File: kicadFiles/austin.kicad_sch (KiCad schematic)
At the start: 553 parts, among them J1 ARM SWD, J2 TYPE-C-31-M12_13, J3 Conn_01x04, Q1 AO3401A, Q2 DTC123JKAT146, Q3 DTC123J, SW1 MXSwitch, SW10 MXSwitch, SW100 MXSwitch, SW101 MXSwitch, SW102 MXSwitch, SW103 MXSwitch, SW104 MXSwitch, SW105 MXSwitch, SW106 MXSwitch, SW107 MXSwitch, SW108 MXSwitch, SW109 MXSwitch, SW11 MXSwitch, SW110 MXSwitch, SW111 MXSwitch, SW112 MXSwitch, SW113 MXSwitch, SW114 MXSwitch, SW12 MXSwitch, SW13 MXSwitch, SW14 MXSwitch, SW15 MXSwitch, SW16 MXSwitch, SW17 MXSwitch, SW18 MXSwitch, SW19 MXSwitch, SW2 MXSwitch, SW20 MXSwitch, SW21 MXSwitch, SW22 MXSwitch, SW23 MXSwitch, SW24 MXSwitch, SW25 MXSwitch, SW26 MXSwitch, SW27 MXSwitch, SW28 MXSwitch, SW29 MXSwitch, SW3 MXSwitch, SW30 MXSwitch, SW31 MXSwitch, SW32 MXSwitch, SW33 MXSwitch, SW34 MXSwitch, SW35 MXSwitch, SW36 MXSwitch, SW37 MXSwitch, SW38 MXSwitch, SW39 MXSwitch, SW4 MXSwitch, SW40 MXSwitch, SW41 MXSwitch, SW42 MXSwitch, SW43 MXSwitch, SW44 MXSwitch, SW45 MXSwitch, SW46 MXSwitch, SW47 MXSwitch, SW48 MXSwitch, SW49 MXSwitch, SW5 MXSwitch, SW50 MXSwitch, SW51 MXSwitch, SW52 MXSwitch, SW53 MXSwitch, SW54 MXSwitch, SW55 MXSwitch, SW56 MXSwitch, SW57 MXSwitch, SW58 MXSwitch, SW59 MXSwitch, SW6 MXSwitch, SW60 MXSwitch, SW61 MXSwitch, SW62 MXSwitch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

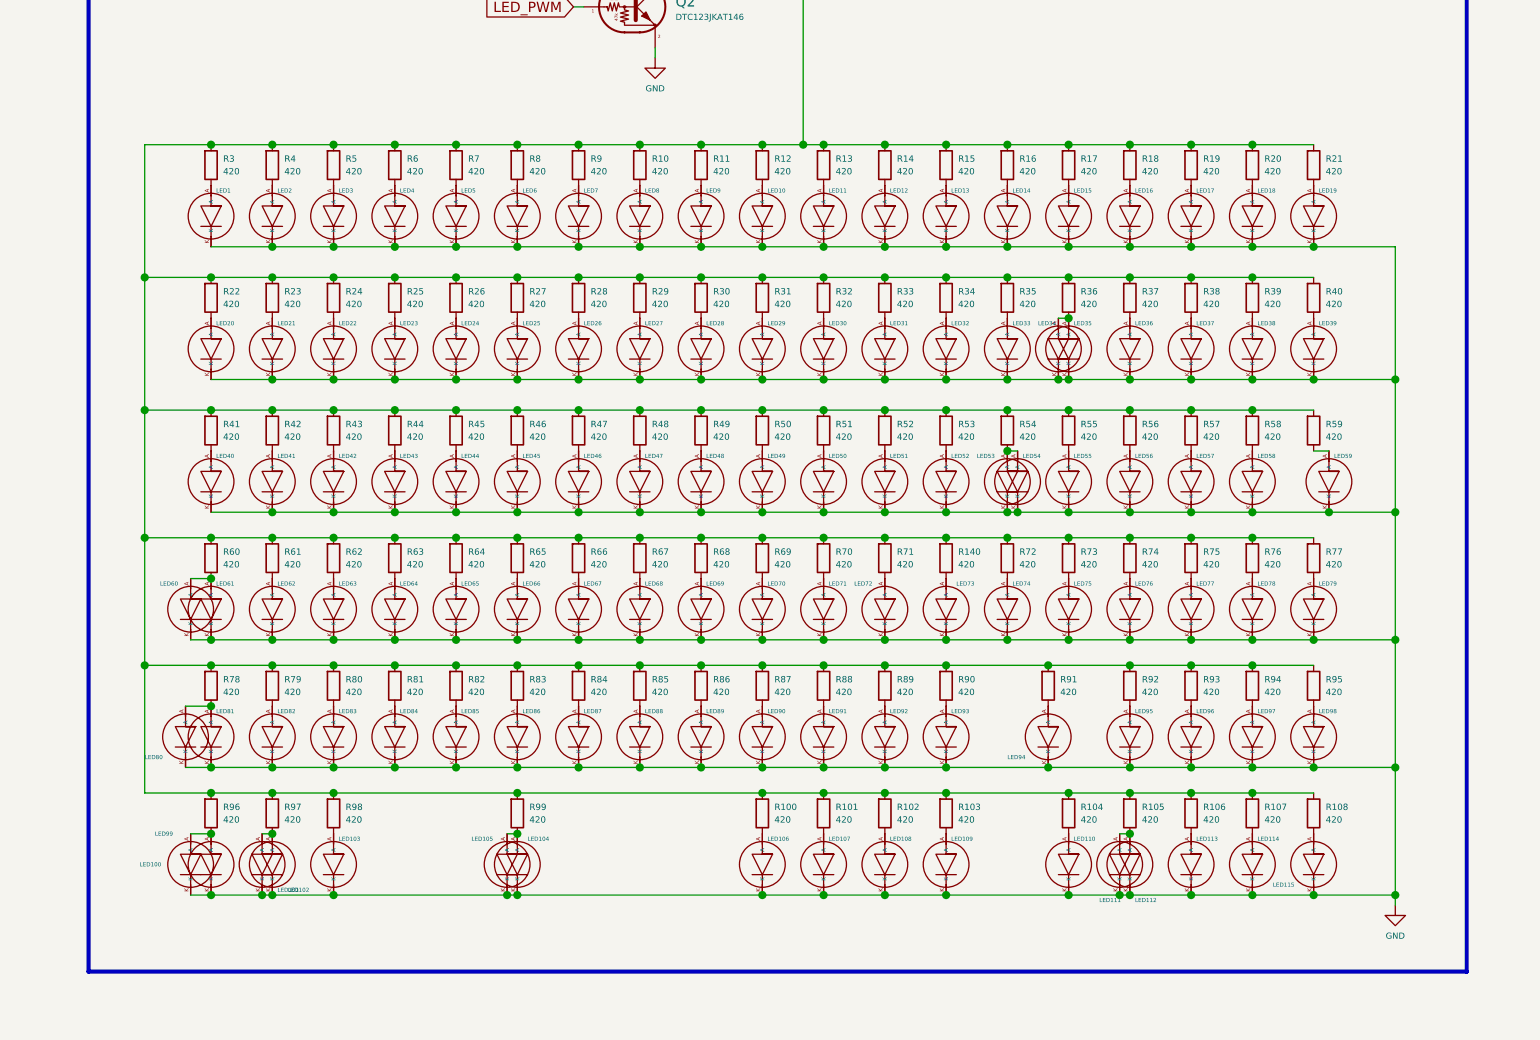
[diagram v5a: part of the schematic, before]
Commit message: "QOL improvements"
- Better in-switch LED tracing with more solid ground pour
- Indicator LEDs changed to 0805 package
- Overall updates on routing
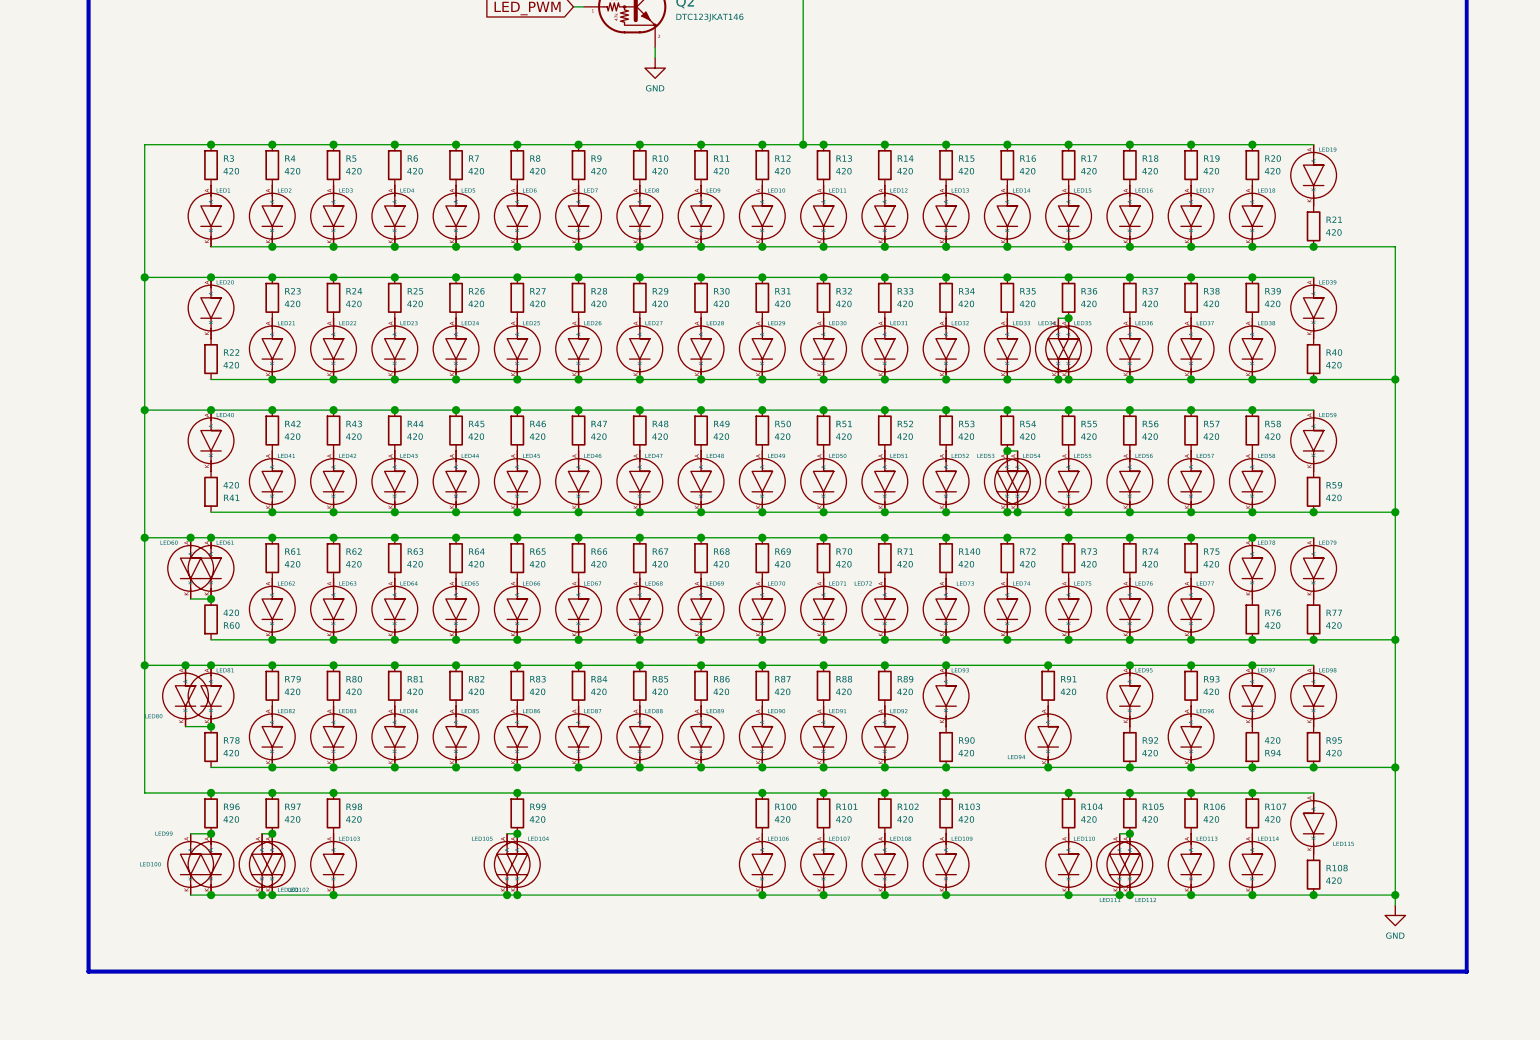
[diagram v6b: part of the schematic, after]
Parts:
- R113, R114, R115: footprint acheronComponents:R_SMD_1206 -> Resistor_SMD:R_0805_2012Metric; Package (none) -> R0805
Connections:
- net GND: now also R108.2, R21.2, R22.2, R40.2, R41.1, R59.2, R60.1, R76.2, R77.2, R78.2, R90.2, R92.2, R94.1, R95.2; no longer LED115.K, LED19.K, LED20.K, LED39.K, LED40.K, LED59.K, LED60.K, LED61.K, LED78.K, LED79.K, LED80.K, LED81.K, LED93.K, LED95.K, LED97.K, LED98.K
- net at Q1.3 (D), R10.1, R100.1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: now also LED115.A, LED19.A, LED20.A, LED39.A, LED40.A, LED59.A, LED60.A, LED61.A, LED78.A, LED79.A, LED80.A, LED81.A, LED93.A, LED95.A, LED97.A, LED98.A; no longer R108.1, R21.1, R22.1, R40.1, R41.1, R59.1, R60.1, R76.1, R77.1, R78.1, R90.1, R92.1, R94.1, R95.1
- net at R41.2: now also LED40.K; no longer LED40.A
- net at R94.2: now also LED97.K; no longer LED97.A
- new net: LED39.K, R40.1
- new net: LED59.K, R59.1
- new net: LED93.K, R90.1
- new net: LED79.K, R77.1
- new net: LED80.K, LED81.K, R78.1
- new net: LED19.K, R21.1
- new net: LED20.K, R22.1
- new net: LED60.K, LED61.K, R60.2
- new net: LED78.K, R76.1
- new net: LED95.K, R92.1
- new net: LED98.K, R95.1
- new net: LED115.K, R108.1
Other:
- moved on the sheet: LED115, LED19, LED20, LED39, LED40, LED59, LED60, LED61, LED78, LED79, LED80, LED81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

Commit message: Add LED polarity indicators, clean routes up
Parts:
- R100: renamed from R69; value 420 -> 470R
- R101: renamed from R70; value 420 -> 470R
- R102: renamed from R71; value 420 -> 470R
- R103: renamed from R140; value 420 -> 470R
- R104: renamed from R72; value 420 -> 470R
- R105: renamed from R73; value 420 -> 470R
- R106: renamed from R74; value 420 -> 470R
- R107: renamed from R75; value 420 -> 470R
- R108: renamed from R76; value 420 -> 470R
- R109: renamed from R77; value 420 -> 470R
- R11: renamed from R120; value 5R -> 4.7R
- R110: renamed from R79; value 420 -> 470R
- R111: renamed from R80; value 420 -> 470R
- R112: renamed from R81; value 420 -> 470R
- R113: renamed from R82; value 420 -> 470R
- R114: renamed from R83; value 420 -> 470R
- R115: renamed from R84; value 420 -> 470R
- R116: renamed from R85; value 420 -> 470R
- R117: renamed from R86; value 420 -> 470R
- R118: renamed from R87; value 420 -> 470R
- R119: renamed from R88; value 420 -> 470R
- R12: renamed from R121; value 5R -> 4.7R
- R120: renamed from R89; value 420 -> 470R
- R121: renamed from R91; value 420 -> 470R
- R122: renamed from R93; value 420 -> 470R
- R123: renamed from R78; value 420 -> 470R
- R124: renamed from R90; value 420 -> 470R
- R125: renamed from R92; value 420 -> 470R
- R126: renamed from R94; value 420 -> 470R
- R127: renamed from R95; value 420 -> 470R
- R128: renamed from R97; value 420 -> 470R
- R129: renamed from R98; value 420 -> 470R
- R13: renamed from R122; value 5R -> 4.7R
- R130: renamed from R99; value 420 -> 470R
- R131: renamed from R100; value 420 -> 470R
- R132: renamed from R101; value 420 -> 470R
- R133: renamed from R102; value 420 -> 470R
- R134: renamed from R103; value 420 -> 470R
- R135: renamed from R104; value 420 -> 470R
- R136: renamed from R105; value 420 -> 470R
- R137: renamed from R106; value 420 -> 470R
- R138: renamed from R107; value 420 -> 470R
- R139: renamed from R96; value 420 -> 470R
- R14: renamed from R123; value 5R -> 4.7R
- R140: renamed from R108; value 420 -> 470R
- R15: renamed from R124; value 5R -> 4.7R
- R16: renamed from R125; value 5R -> 4.7R
- R17: renamed from R126; value 5R -> 4.7R
- R18: renamed from R127; value 5R -> 4.7R
- R19: renamed from R128; value 5R -> 4.7R
- R20: renamed from R129; value 5R -> 4.7R
- R21: renamed from R130; value 5R -> 4.7R
- R22: renamed from R131; value 5R -> 4.7R
- R23: renamed from R132; value 5R -> 4.7R
- R24: renamed from R133; value 5R -> 4.7R
- R25: renamed from R134; value 5R -> 4.7R
- R26: renamed from R135; value 5R -> 4.7R
- R27: renamed from R136; value 5R -> 4.7R
- R28: renamed from R137; value 5R -> 4.7R
- R29: renamed from R138; value 5R -> 4.7R
- R30: renamed from R139; value 5R -> 4.7R
- R32: renamed from R60; value 420 -> 470R
- R35: renamed from R3; value 420 -> 470R
- R36: renamed from R4; value 420 -> 470R
- R37: renamed from R5; value 420 -> 470R
- R38: renamed from R6; value 420 -> 470R
- R39: renamed from R7; value 420 -> 470R
- R40: renamed from R8; value 420 -> 470R
- R41: renamed from R9; value 420 -> 470R
- R42: renamed from R10; value 420 -> 470R
- R43: renamed from R11; value 420 -> 470R
- R44: renamed from R12; value 420 -> 470R
- R45: renamed from R13; value 420 -> 470R
- R46: renamed from R14; value 420 -> 470R
- R47: renamed from R15; value 420 -> 470R
- R48: renamed from R16; value 420 -> 470R
- R49: renamed from R17; value 420 -> 470R
- R5: renamed from R113; value 420 -> 470R
- R50: renamed from R18; value 420 -> 470R
- R51: renamed from R19; value 420 -> 470R
- R52: renamed from R20; value 420 -> 470R
- R53: renamed from R21; value 420 -> 470R
- R54: renamed from R23; value 420 -> 470R
- R55: renamed from R24; value 420 -> 470R
- R56: renamed from R25; value 420 -> 470R
- R57: renamed from R26; value 420 -> 470R
- R58: renamed from R27; value 420 -> 470R
- R59: renamed from R28; value 420 -> 470R
- R6: renamed from R114; value 420 -> 470R
- R60: renamed from R29; value 420 -> 470R
- R61: renamed from R30; value 420 -> 470R
- R62: renamed from R31; value 420 -> 470R
- R63: renamed from R32; value 420 -> 470R
- R64: renamed from R33; value 420 -> 470R
- R65: renamed from R34; value 420 -> 470R
- R66: renamed from R35; value 420 -> 470R
- R67: renamed from R36; value 420 -> 470R
- R68: renamed from R37; value 420 -> 470R
- R69: renamed from R38; value 420 -> 470R
- R7: renamed from R115; value 420 -> 470R
- R70: renamed from R39; value 420 -> 470R
- R71: renamed from R22; value 420 -> 470R
- R72: renamed from R40; value 420 -> 470R
- R73: renamed from R42; value 420 -> 470R
- R74: renamed from R43; value 420 -> 470R
- R75: renamed from R44; value 420 -> 470R
- R76: renamed from R45; value 420 -> 470R
- R77: renamed from R46; value 420 -> 470R
- R78: renamed from R47; value 420 -> 470R
- R79: renamed from R48; value 420 -> 470R
- R80: renamed from R49; value 420 -> 470R
- R81: renamed from R50; value 420 -> 470R
- R82: renamed from R51; value 420 -> 470R
- R83: renamed from R52; value 420 -> 470R
- R84: renamed from R53; value 420 -> 470R
- R85: renamed from R54; value 420 -> 470R
- R86: renamed from R55; value 420 -> 470R
- R87: renamed from R56; value 420 -> 470R
- R88: renamed from R57; value 420 -> 470R
- R89: renamed from R58; value 420 -> 470R
- R90: renamed from R41; value 420 -> 470R
- R91: renamed from R59; value 420 -> 470R
- R92: renamed from R61; value 420 -> 470R
- R93: renamed from R62; value 420 -> 470R
- R94: renamed from R63; value 420 -> 470R
- R95: renamed from R64; value 420 -> 470R
- R96: renamed from R65; value 420 -> 470R
- R97: renamed from R66; value 420 -> 470R
- R98: renamed from R67; value 420 -> 470R
- R99: renamed from R68; value 420 -> 470R
- renumbered D106 to D1, D115 to D10, D76 to D100, D77 to D101, D78 to D102, D79 to D103, D80 to D104, D81 to D105, D82 to D106, D83 to D107, D84 to D108, D85 to D109, D116 to D11, D86 to D110, D87 to D111, D88 to D112, D89 to D113, D90 to D114, D91 to D115, D92 to D116, D93 to D117, D94 to D118, D95 to D119, D117 to D12, D96 to D120, D97 to D121, D98 to D122, D99 to D123, D100 to D124, D101 to D125, D102 to D126, D103 to D127, D105 to D128, D118 to D13, D119 to D14, D120 to D15, D121 to D16, D122 to D17, D123 to D18, D124 to D19, D107 to D2, D125 to D20, D126 to D21, D127 to D22, D128 to D23, D1 to D24, D2 to D25, D3 to D26, D4 to D27, D5 to D28, D6 to D29, D108 to D3, D7 to D30, D8 to D31, D9 to D32, D10 to D33, D11 to D34, D12 to D35, D13 to D36, D14 to D37, D15 to D38, D16 to D39, D109 to D4, D17 to D40, D18 to D41, D19 to D42, D20 to D43, D21 to D44, D22 to D45, D23 to D46, D24 to D47, D25 to D48, D26 to D49, D110 to D5, D27 to D50, D28 to D51, D29 to D52, D30 to D53, D31 to D54, D32 to D55, D33 to D56, D34 to D57, D35 to D58, D36 to D59, D111 to D6, D37 to D60, D38 to D61, D39 to D62, D40 to D63, D41 to D64, D42 to D65, D43 to D66, D44 to D67, D45 to D68, D46 to D69, D112 to D7, D47 to D70, D48 to D71, D49 to D72, D50 to D73, D51 to D74, D52 to D75, D53 to D76, D54 to D77, D55 to D78, D56 to D79, D113 to D8, D104 to D80, D57 to D81, D58 to D82, D59 to D83, D60 to D84, D61 to D85, D62 to D86, D63 to D87, D64 to D88, D65 to D89, D114 to D9, D66 to D90, D67 to D91, D68 to D92, D69 to D93, D70 to D94, D71 to D95, D72 to D96, D73 to D97, D74 to D98, D75 to D99, J3 to J1, J1 to J2, J2 to J3, LED60 to LED1, LED7 to LED10, LED115 to LED101, LED101 to LED102, LED102 to LED103, LED103 to LED104, LED104 to LED105, LED105 to LED106, LED106 to LED107, LED107 to LED108, LED108 to LED109, LED8 to LED11, LED109 to LED110, LED110 to LED111, LED111 to LED112, LED112 to LED113, LED113 to LED114, LED114 to LED115, LED9 to LED12, LED10 to LED13, LED11 to LED14, LED12 to LED15, LED13 to LED16, LED14 to LED17, LED15 to LED18, LED16 to LED19, LED61 to LED2, LED17 to LED20, LED18 to LED21, LED20 to LED22, LED39 to LED23, LED21 to LED24, LED22 to LED25, LED23 to LED26, LED24 to LED27, LED25 to LED28, LED26 to LED29, LED19 to LED3, LED27 to LED30, LED28 to LED31, LED29 to LED32, LED30 to LED33, LED31 to LED34, LED32 to LED35, LED33 to LED36, LED34 to LED37, LED35 to LED38, LED36 to LED39, LED1 to LED4, LED37 to LED40, LED38 to LED41, LED40 to LED42, LED59 to LED43, LED41 to LED44, LED42 to LED45, LED43 to LED46, LED44 to LED47, LED45 to LED48, LED46 to LED49, LED2 to LED5, LED47 to LED50, LED48 to LED51, LED49 to LED52, LED50 to LED53, LED51 to LED54, LED52 to LED55, LED53 to LED56, LED54 to LED57, LED55 to LED58, LED56 to LED59, LED3 to LED6, LED57 to LED60, LED58 to LED61, LED78 to LED62, LED79 to LED63, LED62 to LED64, LED63 to LED65, LED64 to LED66, LED65 to LED67, LED66 to LED68, LED67 to LED69, LED4 to LED7, LED68 to LED70, LED69 to LED71, LED70 to LED72, LED71 to LED73, LED72 to LED74, LED73 to LED75, LED74 to LED76, LED75 to LED77, LED76 to LED78, LED77 to LED79, LED5 to LED8, LED93 to LED82, LED95 to LED83, LED97 to LED84, LED98 to LED85, LED82 to LED86, LED83 to LED87, LED84 to LED88, LED85 to LED89, LED6 to LED9, LED86 to LED90, LED87 to LED91, LED88 to LED92, LED89 to LED93, LED90 to LED94, LED91 to LED95, LED92 to LED96, LED94 to LED97, LED96 to LED98, Q3 to Q1, Q1 to Q2, Q2 to Q3, R111 to R1, R118 to R10, R109 to R2, R110 to R3, R119 to R31, R1 to R33, R2 to R34, R112 to R4, R116 to R8, R117 to R9, S1 to SW1, SW8 to SW10, SW97 to SW100, SW98 to SW101, SW99 to SW102, SW100 to SW103, SW101 to SW104, SW102 to SW105, SW103 to SW106, SW104 to SW107, SW105 to SW108, SW106 to SW109, SW9 to SW11, SW107 to SW110, SW109 to SW111, SW110 to SW112, SW111 to SW113, SW112 to SW114, SW113 to SW115, SW114 to SW116, SW10 to SW12, SW11 to SW13, SW12 to SW14, SW13 to SW15, SW14 to SW16, SW15 to SW17, SW16 to SW18, SW17 to SW19, SW18 to SW20, SW19 to SW21, SW20 to SW22, SW21 to SW23, SW22 to SW24, SW23 to SW25, SW24 to SW26, SW25 to SW27, SW26 to SW28, SW27 to SW29, SW1 to SW3, SW28 to SW30, SW29 to SW31, SW30 to SW32, SW31 to SW33, SW32 to SW34, SW33 to SW35, SW34 to SW36, SW35 to SW37, SW36 to SW38, SW37 to SW39, SW2 to SW4, SW38 to SW40, SW39 to SW41, SW40 to SW42, SW41 to SW43, SW42 to SW44, SW43 to SW45, SW44 to SW46, SW45 to SW47, SW46 to SW48, SW47 to SW49, SW3 to SW5, SW48 to SW50, SW49 to SW51, SW50 to SW52, SW51 to SW53, SW52 to SW54, SW53 to SW55, SW54 to SW56, SW55 to SW57, SW56 to SW58, SW57 to SW59, SW4 to SW6, SW58 to SW60, SW108 to SW61, SW59 to SW62, SW60 to SW63, SW61 to SW64, SW62 to SW65, SW63 to SW66, SW64 to SW67, SW65 to SW68, SW66 to SW69, SW5 to SW7, SW67 to SW70, SW68 to SW71, SW69 to SW72, SW70 to SW73, SW71 to SW74, SW72 to SW75, SW73 to SW76, SW74 to SW77, SW75 to SW78, SW76 to SW79, SW6 to SW8, SW77 to SW80, SW78 to SW81, SW79 to SW82, SW80 to SW83, SW81 to SW84, SW82 to SW85, SW83 to SW86, SW84 to SW87, SW85 to SW88, SW86 to SW89, SW7 to SW9, SW87 to SW90, SW88 to SW91, SW89 to SW92, SW90 to SW93, SW91 to SW94, SW92 to SW95, SW93 to SW96, SW94 to SW97, SW95 to SW98, SW96 to SW99
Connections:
- net GND: now also R139.2; no longer LED100.K, LED99.K
- net LED_SIGNAL: now reaches LED1.A, LED101.A, LED2.A, LED22.A, LED23.A, LED3.A, LED42.A, LED43.A, LED62.A, LED63.A, LED80.A, LED81.A, LED82.A, LED83.A, LED84.A, LED85.A, Q2.3 (D), R100.1, R101.1, R102.1, R103.1, R104.1, R105.1, R106.1, R107.1, R110.1, R111.1, R112.1, R113.1, R114.1, R115.1, R116.1, R117.1, R118.1, R119.1, R120.1, R121.1, R122.1, R128.1, R129.1, R130.1, R131.1, R132.1, R133.1, R134.1, R135.1, R136.1, R137.1, R138.1, R35.1, R36.1, R37.1, R38.1, R39.1, R40.1, R41.1, R42.1, R43.1, R44.1, R45.1, R46.1, R47.1, R48.1, R49.1, R50.1, R51.1, R52.1, R54.1, R55.1, R56.1, R57.1, R58.1, R59.1, R60.1, R61.1, R62.1, R63.1, R64.1, R65.1, R66.1, R67.1, R68.1, R69.1, R70.1, R73.1, R74.1, R75.1, R76.1, R77.1, R78.1, R79.1, R80.1, R81.1, R82.1, R83.1, R84.1, R85.1, R86.1, R87.1, R88.1, R89.1, R92.1, R93.1, R94.1, R95.1, R96.1, R97.1, R98.1, R99.1
- net LED_SIGNAL: now also LED100.A, LED99.A; no longer R139.1
- new net: LED100.K, LED99.K, R139.1
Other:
- moved on the sheet: C1, C10, C11, C12, C13, C14, C15, C16, C17, C18, C19, C2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

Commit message: QOL upgrades
- Indicators are now brightness modulated with the LED matrix
- Added warning signs for washer usage on potential stab screws/switch pads short circuits
- Updated differential pair routing
- Caps Lock LED can be used as indicator or LED
- Above-arrows indicators are now triangulated
- Updated layout labelling
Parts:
- added GR1, GR2, GR3, GR4: Warning sign, acheron_Graphics:warning_sign_3.6x3.2mm, symbol Mechanical:MountingHole
- added SW2: PCM12SMTR, Button_Switch_SMD:SW_SPDT_PCM12, symbol Switch:SW_SPDT
- J3: value TYPE-C-31-M12_13 -> TYPE-C-31-M12
- R1, R4: footprint Resistor_SMD:R_0402_1005Metric -> Resistor_SMD:R_0805_2012Metric; Package (none) -> R0805
- R2, R3: footprint acheronComponents:R_SMD_1206 -> Resistor_SMD:R_0805_2012Metric; Package (none) -> R0805
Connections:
- net 3V3: now also C14.1; no longer C14.2
- net 5V: no longer LEDCAPS1.A, LEDNUM1.A, LEDSCR1.A
- net GND: now also C14.2, SW2.1 (A); no longer C14.1, R32.1
- net INDICATOR3: now also SW2.3 (C)
- net LED_SIGNAL: now also LEDCAPS1.A, LEDNUM1.A, LEDSCR1.A
- new net: R32.1, SW2.2 (B)
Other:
- moved on the sheet: C14, C15, C16, C17, C18, C19, C20, C21, C22, C23, C24, C25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
